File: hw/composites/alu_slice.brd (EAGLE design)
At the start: 50 x 50 mm, 14 parts

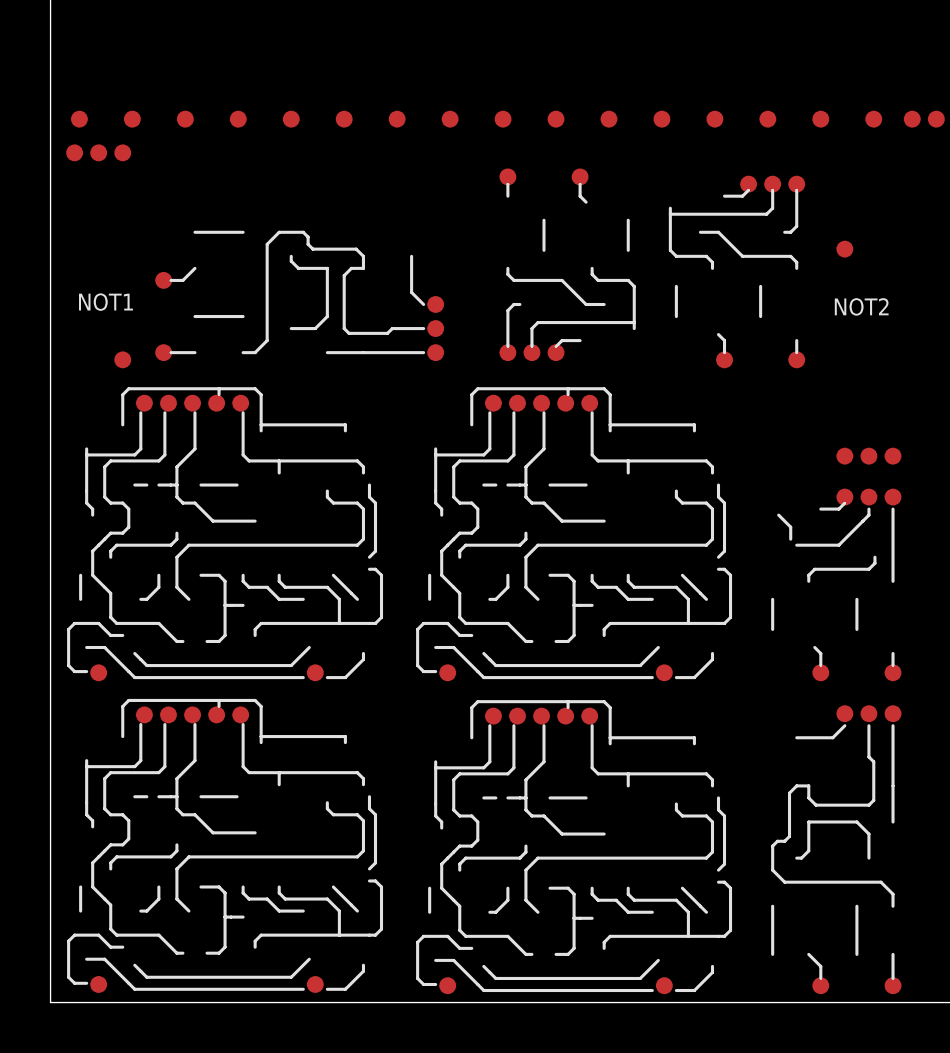
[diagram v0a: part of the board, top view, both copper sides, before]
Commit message: Started changing alu to new format.
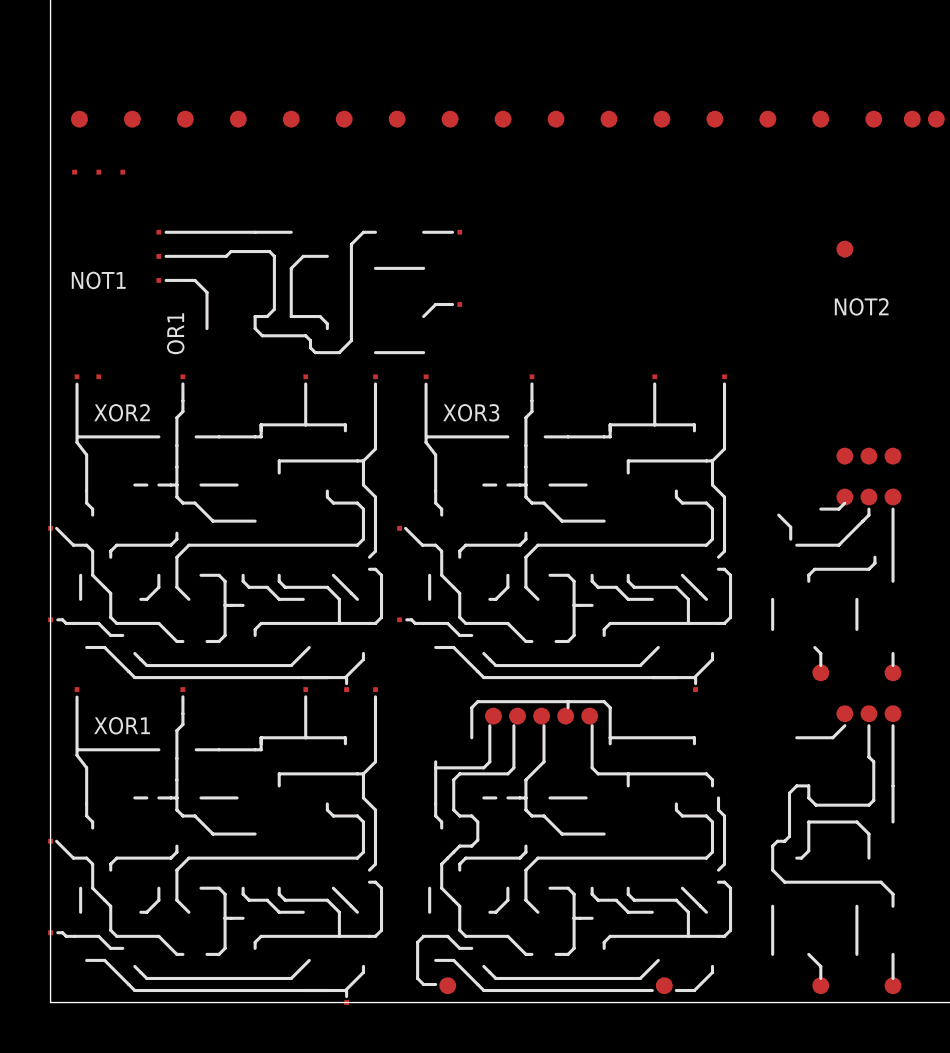
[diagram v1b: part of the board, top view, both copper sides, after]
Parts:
- removed AND1, AND2: AND-UNBUF, p.peter-logic:AND-2-UNBUF
- NOT1: value NOT-VERTICAL -> NOTVERTICAL; device p.peter-logic:NOT-VERTICAL -> p.peter-gator:NOT-VERTICAL
- OR1: device p.peter-logic:OR-2 -> p.peter-gator:OR
- XOR1, XOR2: value EX-XOR -> XOR; device p.peter-logic:XOR-2-EX2 -> p.peter-gator:XOR
- XOR3: device p.peter-logic:XOR-2-EX2 -> p.peter-gator:XOR
- moved XOR2 22.7 mm to (0.00, 13.0)
- moved XOR1 20.8 mm to (0.00, 0.00)
- moved XOR3 9.70 mm to (14.5, 13.0)
- moved OR1 7.38 mm to (17.0, 26.0), turned to 90 degrees
- moved NOT1 5.39 mm to (0.00, 26.0)
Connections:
- removed net N$1: NOT1.IN, OR1.A, XOR1.OUT2
- removed net N$2: OR1.B, XOR2.OUT2
- new net N$6: NOT1.A, OR1.B, XOR2.AND
- new net N$8: OR1.A, XOR3.AND
- net +5V: now also NOT1.V+, OR1.V+, XOR1.V+, XOR2.V+, XOR3.V+; no longer AND1.OUT3, AND2.OUT3, NAND1.OUT1, NOT1.OUT3, NOT2.OUT3, OR1.OUT3, OR2.OUT3, SEL1.V+, SEL2.V+, SEL3.V+, XOR1.OUT1, XOR2.OUT1, XOR3.OUT1, XOR4.OUT1
- net A: now also XOR2.A; no longer XOR1.B
- net B: now also XOR1.A; no longer XOR3.A
- net B_INT: now also XOR1.XOR, XOR2.B; no longer XOR1.A, XOR3.OUT4
- net CARRY: now also XOR3.XOR; no longer XOR2.OUT4
- net CARRY_IN: now also XOR3.A; no longer XOR2.A
- net GND: now also NOT1.V-, OR1.V-, XOR1.V-, XOR2.V-, XOR3.V-; no longer AND1.OUT1, AND2.OUT1, NAND1.OUT3, NOT1.OUT2, NOT2.OUT2, OR1.OUT2, OR2.OUT2, SEL1.GND, SEL2.GND, SEL3.GND, XOR1.OUT5, XOR2.OUT5, XOR3.OUT5, XOR4.OUT5
- net INV_ADD: now also XOR1.B; no longer XOR3.B
- net NAND: now also NOT1.NOT; no longer NOT1.OUT1
- net NOR: now also XOR2.NOR; no longer XOR1.OUT3
- net SUM: now also OR1.OR; no longer OR1.OUT1
- net XOR: now also XOR2.XOR, XOR3.B; no longer XOR1.OUT4, XOR2.B

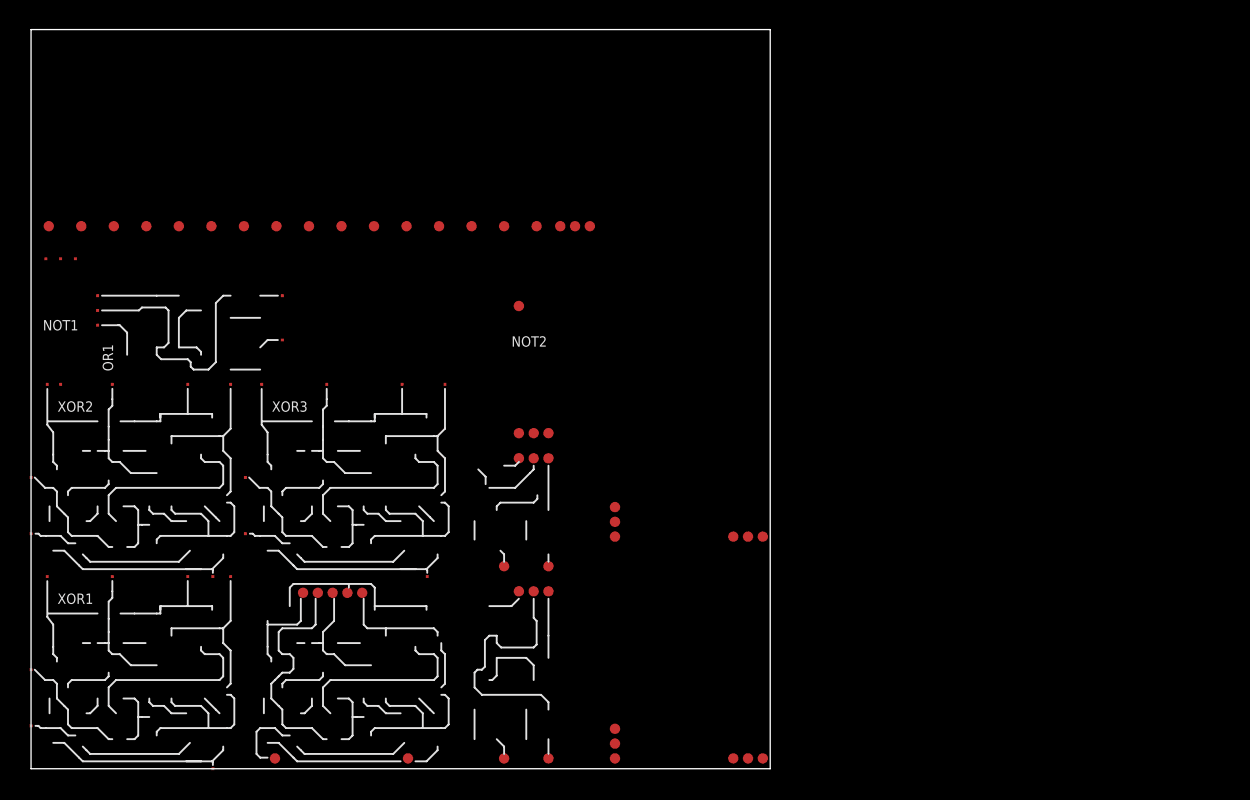
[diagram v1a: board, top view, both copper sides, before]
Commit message: Updated gates to be centered
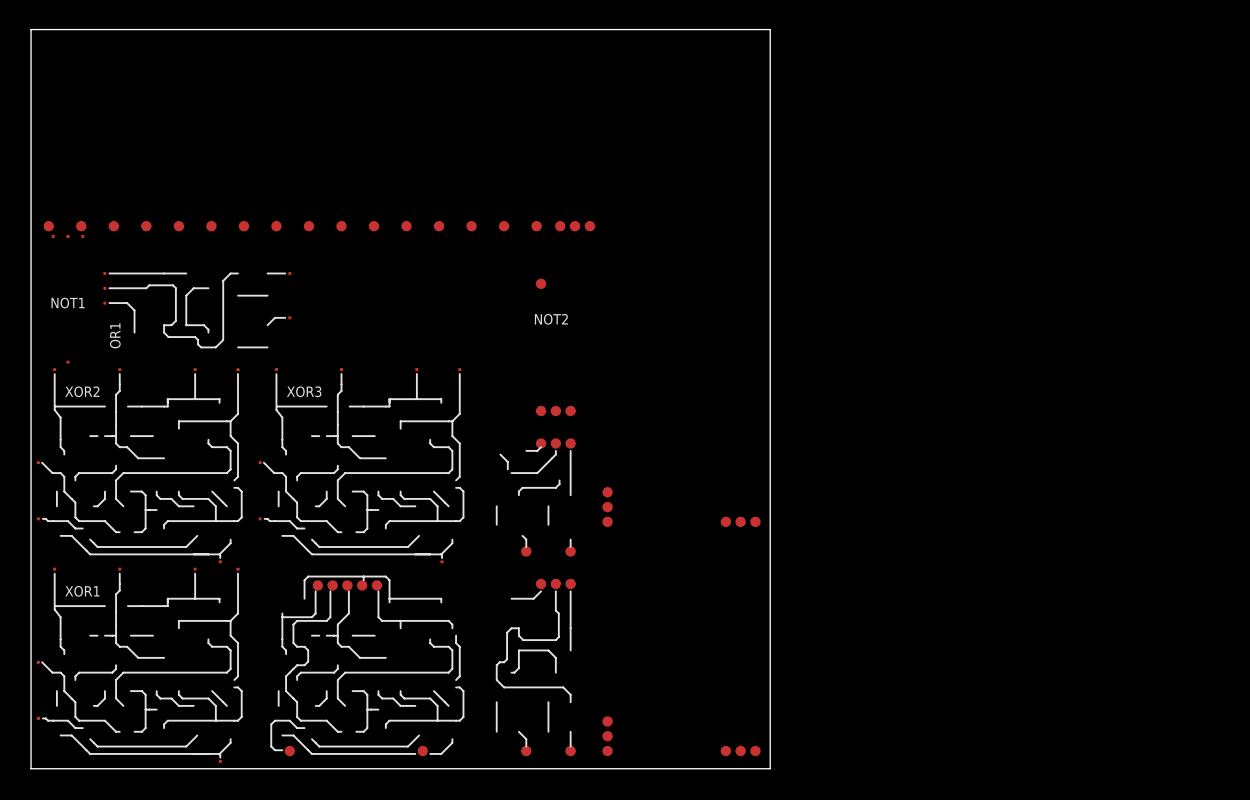
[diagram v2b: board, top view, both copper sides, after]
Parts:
- moved NOT2 2.12 mm to (35.5, 28.5)
- moved NAND1 1.80 mm to (34.0, 18.5)
- moved NOT1 1.58 mm to (0.50, 27.5)
- moved OR1 1.58 mm to (17.5, 27.5)
- moved OR2 1.58 mm to (34.0, 7.00)
- moved XOR3 1.41 mm to (15.5, 14.0)
- moved SEL2 1.12 mm to (38.0, 16.0)
- moved XOR2 1.12 mm to (0.50, 14.0)
- moved XOR4 1.12 mm to (22.8, 7.00)
- moved SEL3 0.71 mm to (38.0, 0.50)
- moved XOR1 0.71 mm to (0.50, 0.50)
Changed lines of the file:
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@@
 </autorouter>
 <elements>
-<element name="XOR4" library="p.peter-logic" package="XOR-2-EX2" value="XOR" x="21.75" y="6.5"/>
-<element name="NOT2" library="p.peter-logic" package="NOT-VERTICAL" value="NOT-VERTICAL" x="34" y="27" rot="R180"/>
+<element name="XOR4" library="p.peter-logic" package="XOR-2-EX2" value="XOR" x="22.75" y="7"/>
+<element name="NOT2" library="p.peter-logic" package="NOT-VERTICAL" value="NOT-VERTICAL" x="35.5" y="28.5" rot="R180"/>
 <element name="SEL1" library="p.peter-logic" package="SELECTOR-8_BIT-NOMUX" value="SELECTOR" x="0" y="36"/>
-<element name="OR2" library="p.peter-logic" package="OR-2" value="OR" x="32.5" y="6.5"/>
-<element name="SEL2" library="p.peter-logic" package="SELECTOR-2-LANE-NOMUX" value="" x="38.5" y="15"/>
-<element name="NAND1" library="p.peter-logic" package="NAND-2" value="NAND" x="32.5" y="17.5"/>
-<element name="SEL3" library="p.peter-logic" package="SELECTOR-2-LANE-NOMUX" value="" x="38.5" y="0"/>
-<element name="XOR1" library="p.peter-gator" package="XOR" value="XOR" x="0" y="0"/>
-<element name="XOR2" library="p.peter-gator" package="XOR" value="XOR" x="0" y="13"/>
-<element name="XOR3" library="p.peter-gator" package="XOR" value="XOR" x="14.5" y="13"/>
-<element name="NOT1" library="p.peter-gator" package="NOT-VERTICAL" value="NOTVERTICAL" x="0" y="26"/>
-<element name="OR1" library="p.peter-gator" package="OR" value="OR" x="17" y="26" rot="R90"/>
+<element name="OR2" library="p.peter-logic" package="OR-2" value="OR" x="34" y="7"/>
+<element name="SEL2" library="p.peter-logic" package="SELECTOR-2-LANE-NOMUX" value="" x="38" y="16"/>
+<element name="NAND1" library="p.peter-logic" package="NAND-2" value="NAND" x="34" y="18.5"/>
+<element name="SEL3" library="p.peter-logic" package="SELECTOR-2-LANE-NOMUX" value="" x="38" y="0.5"/>
+<element name="XOR1" library="p.peter-gator" package="XOR" value="XOR" x="0.5" y="0.5"/>
+<element name="XOR2" library="p.peter-gator" package="XOR" value="XOR" x="0.5" y="14"/>
+<element name="XOR3" library="p.peter-gator" package="XOR" value="XOR" x="15.5" y="14"/>
+<element name="NOT1" library="p.peter-gator" package="NOT-VERTICAL" value="NOTVERTICAL" x="0.5" y="27.5"/>
+<element name="OR1" library="p.peter-gator" package="OR" value="OR" x="17.5" y="27.5" rot="R90"/>
 </elements>
 <signals>
@@
 <contactref element="SEL3" pad="IN2"/>
 <contactref element="XOR2" pad="A"/>
-<wire x1="12.3" y1="13" x2="39.5" y2="2.7" width="0" layer="19" extent="1-1"/>
-<wire x1="3.4" y1="36.7" x2="12.3" y2="13" width="0" layer="19" extent="1-1"/>
+<wire x1="12.8" y1="14" x2="39" y2="3.2" width="0" layer="19" extent="1-1"/>
+<wire x1="3.4" y1="36.7" x2="12.8" y2="14" width="0" layer="19" extent="1-1"/>
 </signal>
 <signal name="XOR">
@@
 <contactref element="XOR3" pad="B"/>
 <contactref element="XOR2" pad="XOR"/>
-<wire x1="10.6" y1="26" x2="16.6" y2="36.7" width="0" layer="19" extent="1-1"/>
-<wire x1="14.5" y1="15.9" x2="10.6" y2="26" width="0" layer="19" extent="1-1"/>
+<wire x1="11.1" y1="27" x2="16.6" y2="36.7" width="0" layer="19" extent="1-1"/>
+<wire x1="15.5" y1="16.9" x2="11.1" y2="27" width="0" layer="19" extent="1-1"/>
 </signal>
 <signal name="CARRY_IN">
@@
 <contactref element="OR2" pad="A"/>
 <contactref element="OR1" pad="OR"/>
-<wire x1="4.5" y1="30" x2="21" y2="36.7" width="0" layer="19" extent="1-1"/>
-<wire x1="32" y1="0.7" x2="21" y2="36.7" width="0" layer="19" extent="1-1"/>
+<wire x1="5" y1="31.5" x2="21" y2="36.7" width="0" layer="19" extent="1-1"/>
+<wire x1="33.5" y1="1.2" x2="21" y2="36.7" width="0" layer="19" extent="1-1"/>
 </signal>
 <signal name="CARRY">
@@
 <contactref element="XOR3" pad="V+"/>
 <contactref element="OR1" pad="V+"/>
-<wire x1="4.5" y1="32" x2="15.6" y2="26" width="0" layer="19" extent="1-1"/>
-<wire x1="3" y1="34.5" x2="4.5" y2="32" width="0" layer="19" extent="1-1"/>
-<wire x1="1.1" y1="26" x2="4.5" y2="32" width="0" layer="19" extent="1-1"/>
-<wire x1="1.1" y1="13" x2="1.1" y2="26" width="0" layer="19" extent="1-1"/>
+<wire x1="5" y1="33.5" x2="16.6" y2="27" width="0" layer="19" extent="1-1"/>
+<wire x1="3.5" y1="36" x2="5" y2="33.5" width="0" layer="19" extent="1-1"/>
+<wire x1="1.6" y1="27" x2="5" y2="33.5" width="0" layer="19" extent="1-1"/>
+<wire x1="1.6" y1="13.5" x2="1.6" y2="27" width="0" layer="19" extent="1-1"/>
 </signal>
 <signal name="GND">
@@
 <contactref element="XOR3" pad="V-"/>
 <contactref element="OR1" pad="V-"/>
-<wire x1="13.5" y1="26" x2="28" y2="26" width="0" layer="19" extent="1-1"/>
-<wire x1="4.5" y1="31" x2="13.5" y2="26" width="0" layer="19" extent="1-1"/>
-<wire x1="2" y1="34.5" x2="4.5" y2="31" width="0" layer="19" extent="1-1"/>
-<wire x1="13.5" y1="13" x2="13.5" y2="26" width="0" layer="19" extent="1-1"/>
+<wire x1="14" y1="27" x2="29" y2="27" width="0" layer="19" extent="1-1"/>
+<wire x1="5" y1="32.5" x2="14" y2="27" width="0" layer="19" extent="1-1"/>
+<wire x1="2.5" y1="36" x2="5" y2="32.5" width="0" layer="19" extent="1-1"/>
+<wire x1="14" y1="13.5" x2="14" y2="27" width="0" layer="19" extent="1-1"/>
 </signal>
 <signal name="NOR">
 <contactref element="SEL1" pad="IN3"/>
 <contactref element="XOR2" pad="NOR"/>
-<wire x1="5.5" y1="26" x2="12.2" y2="36.7" width="0" layer="19" extent="1-1"/>
+<wire x1="6" y1="27" x2="12.2" y2="36.7" width="0" layer="19" extent="1-1"/>
 </signal>
 <signal name="NAND">
 <contactref element="SEL1" pad="IN2"/>
 <contactref element="NOT1" pad="NOT"/>
-<wire x1="1" y1="34.5" x2="7.8" y2="36.7" width="0" layer="19" extent="1-1"/>
+<wire x1="1.5" y1="36" x2="7.8" y2="36.7" width="0" layer="19" extent="1-1"/>
 </signal>
 <signal name="B_INT">
 <contactref element="XOR1" pad="XOR"/>
 <contactref element="XOR2" pad="B"/>
-<wire x1="0" y1="15.9" x2="10.6" y2="13" width="0" layer="19" extent="1-1"/>
+<wire x1="0.5" y1="16.9" x2="11.1" y2="13.5" width="0" layer="19" extent="1-1"/>
 </signal>
 <signal name="B">
 <contactref element="SEL1" pad="IN8"/>
 <contactref element="XOR1" pad="A"/>
-<wire x1="12.3" y1="0" x2="34.2" y2="36.7" width="0" layer="19" extent="1-1"/>
+<wire x1="12.8" y1="0.5" x2="34.2" y2="36.7" width="0" layer="19" extent="1-1"/>
 </signal>
 <signal name="OUT">
 <contactref element="XOR4" pad="A"/>
 <contactref element="SEL1" pad="OUT"/>
-<wire x1="16.5" y1="0.7" x2="36.8" y2="36.7" width="0" layer="19" extent="1-1"/>
+<wire x1="17.5" y1="1.2" x2="36.8" y2="36.7" width="0" layer="19" extent="1-1"/>
 </signal>
 <signal name="OUT_INV">
@@
 <contactref element="SEL2" pad="SEL"/>
 <contactref element="NOT2" pad="IN"/>
-<wire x1="39.5" y1="15.7" x2="33" y2="31.3" width="0" layer="19" extent="1-1"/>
+<wire x1="39" y1="16.7" x2="34.5" y2="32.8" width="0" layer="19" extent="1-1"/>
 </signal>
 <signal name="INV_ADD">
@@
 <contactref element="SEL1" pad="IN7"/>
 <contactref element="SEL3" pad="IN1"/>
-<wire x1="39.5" y1="16.7" x2="29.8" y2="36.7" width="0" layer="19" extent="1-1"/>
-<wire x1="39.5" y1="1.7" x2="39.5" y2="16.7" width="0" layer="19" extent="1-1"/>
+<wire x1="39" y1="17.7" x2="29.8" y2="36.7" width="0" layer="19" extent="1-1"/>
+<wire x1="39" y1="2.2" x2="39" y2="17.7" width="0" layer="19" extent="1-1"/>
 </signal>
 <signal name="SEL_ID">
@@
 <contactref element="SEL1" pad="SEL6"/>
 <contactref element="NAND1" pad="A"/>
-<wire x1="32" y1="13.7" x2="23.2" y2="36.7" width="0" layer="19" extent="1-1"/>
+<wire x1="33.5" y1="14.7" x2="23.2" y2="36.7" width="0" layer="19" extent="1-1"/>
 </signal>
 <signal name="SEL_CMP">
 <contactref element="SEL1" pad="SEL7"/>
 <contactref element="SEL3" pad="SEL"/>
-<wire x1="39.5" y1="0.7" x2="27.6" y2="36.7" width="0" layer="19" extent="1-1"/>
+<wire x1="39" y1="1.2" x2="27.6" y2="36.7" width="0" layer="19" extent="1-1"/>
 </signal>
 <signal name="SEL_LOAD">
@@
 <contactref element="SEL1" pad="IN6"/>
 <contactref element="SEL2" pad="OUT"/>
-<wire x1="25.4" y1="36.7" x2="48.5" y2="15.7" width="0" layer="19" extent="1-1"/>
+<wire x1="25.4" y1="36.7" x2="48" y2="16.7" width="0" layer="19" extent="1-1"/>
 </signal>
 <signal name="RIGHT_IN">
@@
 <contactref element="NAND1" pad="OUT2"/>
 <contactref element="XOR4" pad="B"/>
-<wire x1="25.5" y1="0.7" x2="34" y2="21" width="0" layer="19" extent="1-1"/>
+<wire x1="26.5" y1="1.2" x2="35.5" y2="22" width="0" layer="19" extent="1-1"/>
 </signal>
 <signal name="N$5">
 <contactref element="NAND1" pad="B"/>
 <contactref element="NOT2" pad="OUT1"/>
-<wire x1="35" y1="13.7" x2="35" y2="22.7" width="0" layer="19" extent="1-1"/>
+<wire x1="36.5" y1="14.7" x2="36.5" y2="24.2" width="0" layer="19" extent="1-1"/>
 </signal>
 <signal name="RIGHT_OUT">
@@
 <contactref element="XOR2" pad="AND"/>
 <contactref element="NOT1" pad="A"/>
-<wire x1="2" y1="26" x2="17" y2="32" width="0" layer="19" extent="1-1"/>
-<wire x1="0" y1="19.7" x2="2" y2="26" width="0" layer="19" extent="1-1"/>
+<wire x1="2.5" y1="27.5" x2="17.5" y2="33.5" width="0" layer="19" extent="1-1"/>
+<wire x1="0.5" y1="20.7" x2="2.5" y2="27.5" width="0" layer="19" extent="1-1"/>
 </signal>
 <signal name="N$8">
 <contactref element="XOR3" pad="AND"/>
 <contactref element="OR1" pad="A"/>
-<wire x1="14.5" y1="19.7" x2="17" y2="29" width="0" layer="19" extent="1-1"/>
+<wire x1="15.5" y1="20.7" x2="17.5" y2="30.5" width="0" layer="19" extent="1-1"/>
 </signal>
 </signals>
